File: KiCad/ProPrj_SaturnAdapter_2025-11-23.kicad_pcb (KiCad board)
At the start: 2 copper layers, 51 x 32 mm, 33 parts

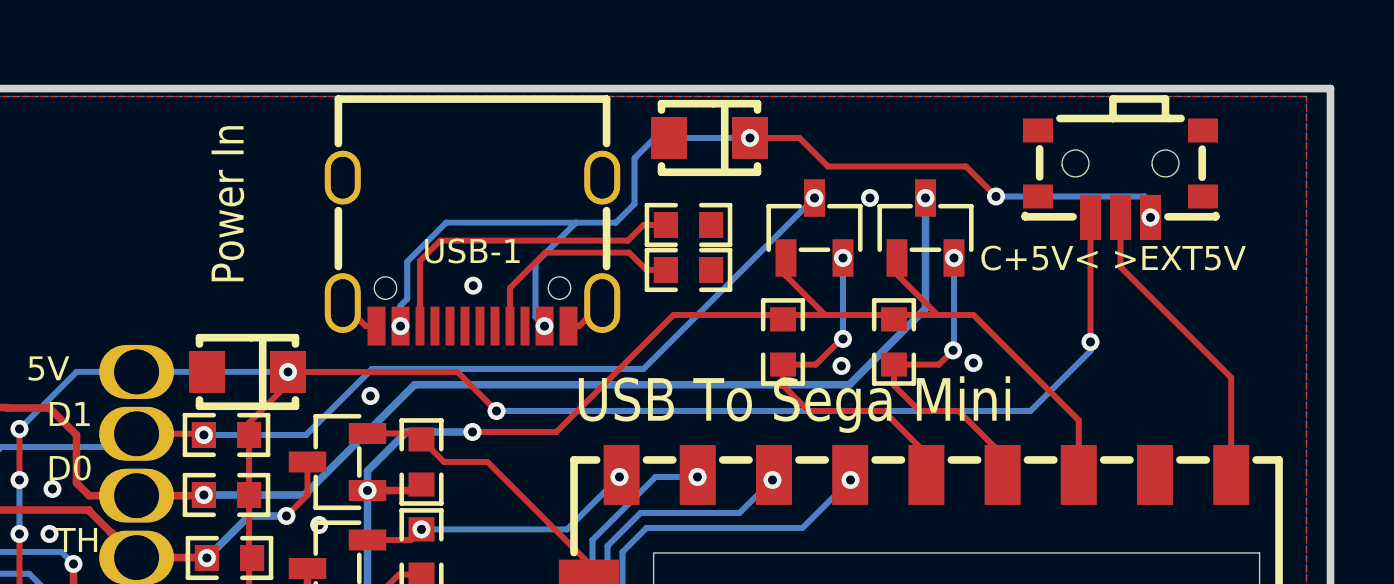
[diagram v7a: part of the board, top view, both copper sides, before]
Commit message: Edits to files to facilitate prototype production, incl. gerbers.
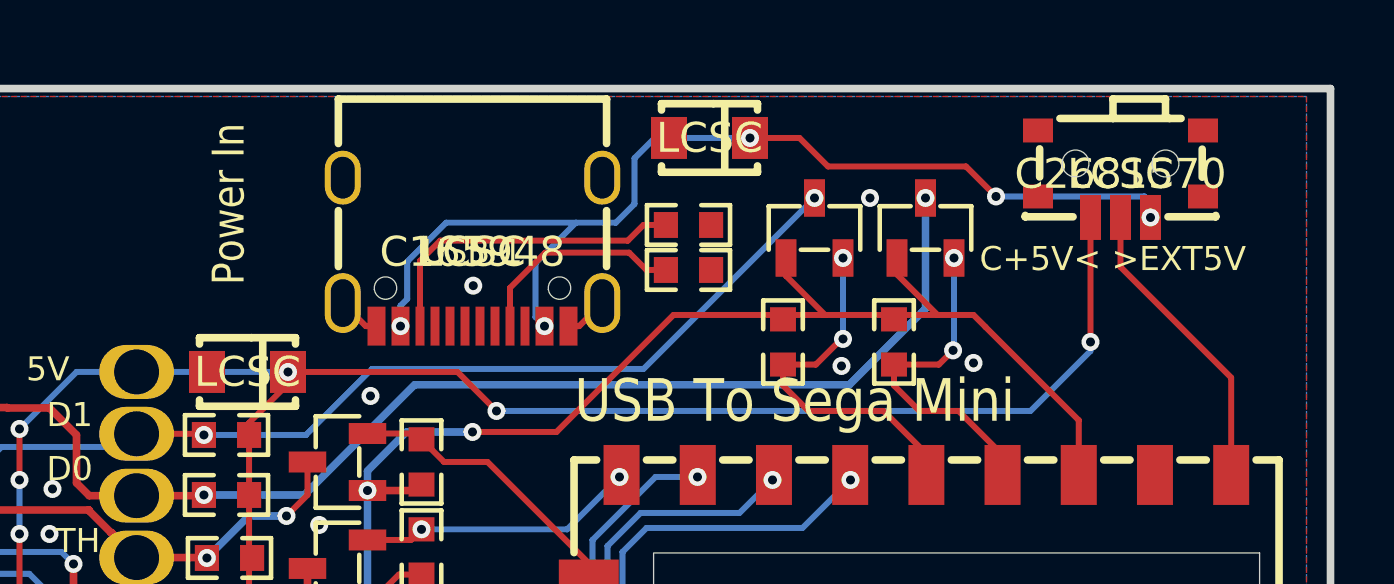
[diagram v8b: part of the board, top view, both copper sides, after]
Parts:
- C1, C2: value (none) -> 10uF
- R1, R10, R11, R12, R13, R14, R2, R3, R4, R5, R6, R7, R8, R9: value (none) -> 10kΩr
- R15, R16: value (none) -> 5.1kΩ
